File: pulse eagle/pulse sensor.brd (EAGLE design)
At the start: 12.4 x 25.4 mm, 8 parts

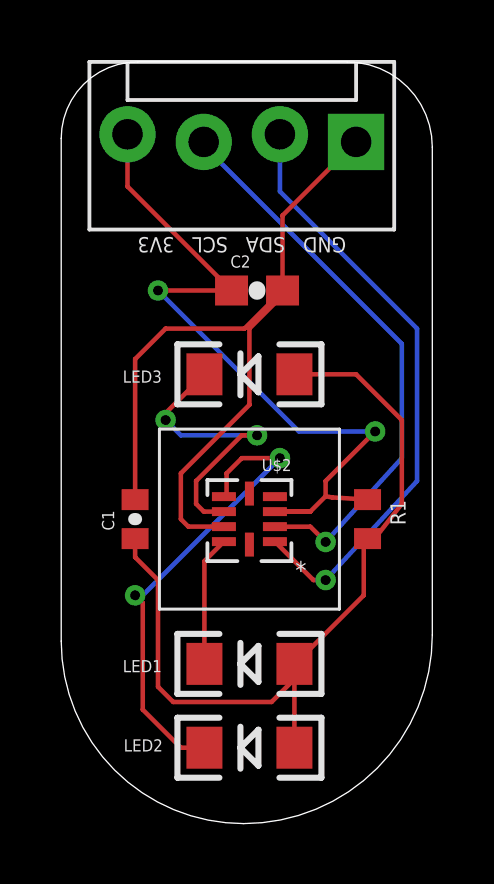
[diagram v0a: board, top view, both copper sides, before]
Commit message: Revision 2 of the pulse sensor. Upgrading to tantalum cap, switching the two caps, and using the correct resistor value. Also switching to temrinal connectors on bottom of board.
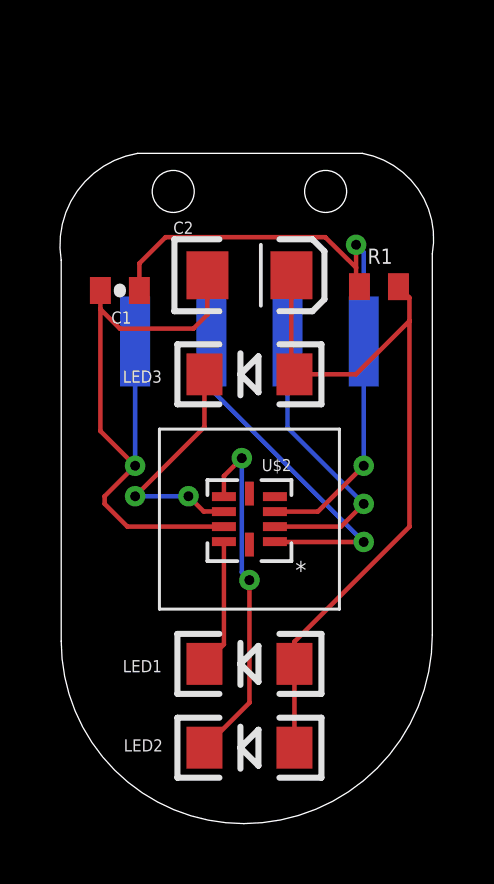
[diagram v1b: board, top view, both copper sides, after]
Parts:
- C2: value 15uF -> 22uF; device SparkFun-Capacitors:0603-CAP -> SparkFun-Passives:EIA3216
- R1: value 1.5k -> 30
- SL2: device SparkFun-Connectors:MOLEX-1X4_LOCK -> SparkFun-Connectors:1X04-SMD
- moved R1 7.76 mm to (10.7, 17.9), turned to 0 degrees
- moved C1 7.64 mm to (2.03, 17.8), turned to 180 degrees
- moved SL2 3.98 mm to (6.35, 21.1), flipped to the bottom
- moved C2 0.57 mm to (6.35, 18.3)
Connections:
- net 3V3: now also C1.1; no longer C2.1
- net GND: now also C2.C; no longer C2.2
- net N$2: now also C2.A; no longer C1.1
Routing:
- net SCL: track 19.0 -> 9.74 mm
- net SDA: track 20.2 -> 11.9 mm
- net GND: track 27.1 -> 21.8 mm, vias 0 -> 1
- net LED2: track 16.0 -> 11.9 mm
- net 3V3: track 25.6 -> 21.6 mm
- net LED3: track 9.78 -> 8.19 mm
- net N$2: track 27.0 -> 26.0 mm
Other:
- board size 12.4 x 25.4 mm -> 12.5 x 22.3 mm
- board text added: "Pulse & Bloom - Sensor 17 July 2014 - Rev. 2"
- board text removed: "Pulse & Bloom - Sensor 20 June 2014 - Rev. 1"
